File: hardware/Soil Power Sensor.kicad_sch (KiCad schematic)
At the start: 0 parts

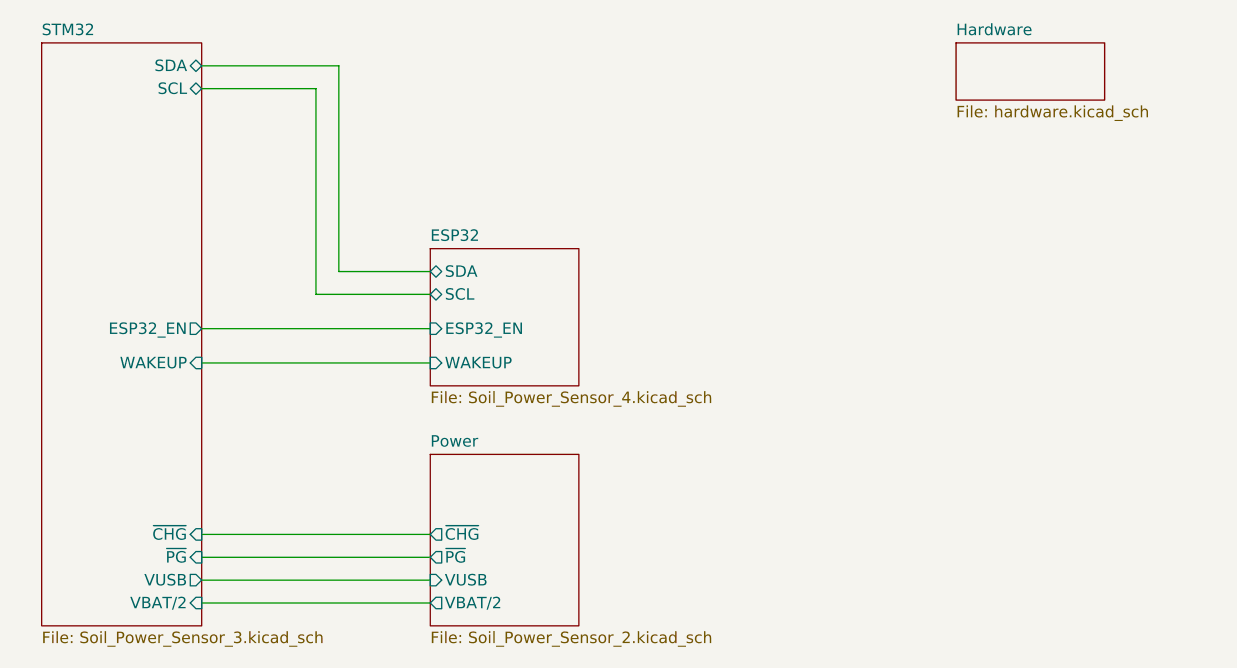
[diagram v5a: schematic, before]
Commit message: lower power buck-boost
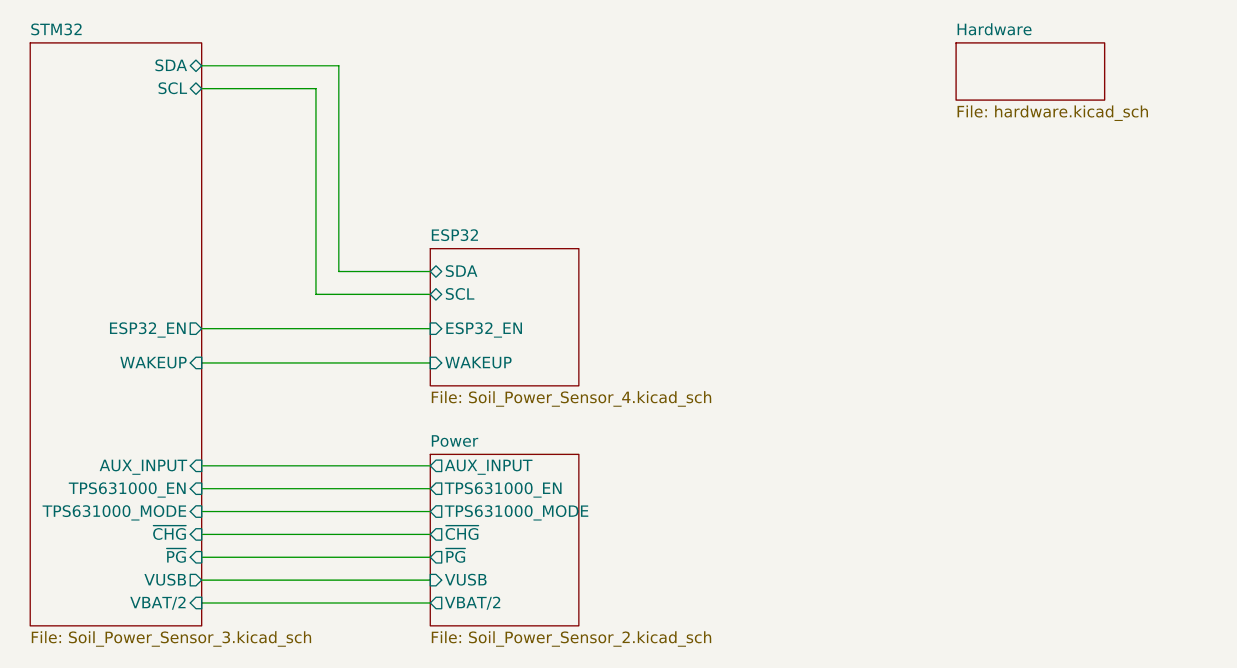
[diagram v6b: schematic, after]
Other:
- sheet Power ports: added AUX_INPUT, TPS631000_EN, TPS631000_MODE; removed none
- sheet STM32 ports: added AUX_INPUT, TPS631000_EN, TPS631000_MODE; removed none
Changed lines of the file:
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@@
+	(wire
+		(pts
+			(xy 137.16 119.38) (xy 162.56 119.38)
+		)
+		(stroke
+			(width 0)
+			(type default)
+		)
+	)
 	(wire
 		(pts
@@
 	(wire
 		(pts
+			(xy 137.16 121.92) (xy 162.56 121.92)
+		)
+		(stroke
+			(width 0)
+			(type default)
+		)
+	)
+	(wire
+		(pts
 			(xy 162.56 100.33) (xy 149.86 100.33)
 		)
@@
 		(pts
 			(xy 137.16 74.93) (xy 152.4 74.93)
+		)
+		(stroke
+			(width 0)
+			(type default)
+		)
+	)
+	(wire
+		(pts
+			(xy 137.16 124.46) (xy 162.56 124.46)
 		)
 		(stroke
@@
 	)
 	(sheet
-		(at 119.38 72.39)
-		(size 17.78 64.77)
+		(at 118.11 72.39)
+		(size 19.05 64.77)
 		(exclude_from_sim no)
 		(in_bom yes)
@@
 		)
 		(property "Sheetname" "STM32"
-			(at 119.38 71.6784 0)
+			(at 118.11 71.6784 0)
 			(effects
 				(font
@@
 		)
 		(property "Sheetfile" "Soil_Power_Sensor_3.kicad_sch"
-			(at 119.38 137.7446 0)
+			(at 118.11 137.7446 0)
 			(effects
 				(font
@@
 		(pin "VBAT{slash}2" input
 			(at 137.16 134.62 0)
+			(effects
+				(font
+					(size 1.27 1.27)
+				)
+				(justify right)
+			)
+		)
+		(pin "TPS631000_EN" input
+			(at 137.16 121.92 0)
+			(effects
+				(font
+					(size 1.27 1.27)
+				)
+				(justify right)
+			)
+		)
+		(pin "TPS631000_MODE" input
+			(at 137.16 124.46 0)
+			(effects
+				(font
+					(size 1.27 1.27)
+				)
+				(justify right)
+			)
+		)
+		(pin "AUX_INPUT" input
+			(at 137.16 119.38 0)
 			(effects
 				(font
@@
 			(effects
 				(font
+					(size 1.27 1.27)
+				)
+				(justify left)
+			)
+		)
+		(pin "TPS631000_EN" output
+			(at 162.56 121.92 180)
+			(effects
+				(font
+					(size 1.27 1.27)
+				)
+				(justify left)
+			)
+		)
+		(pin "TPS631000_MODE" output
+			(at 162.56 124.46 180)
+			(effects
+				(font
+					(size 1.27 1.27)
+				)
+				(justify left)
+			)
+		)
+		(pin "AUX_INPUT" output
+			(at 162.56 119.38 180)
+			(effects
+				(font

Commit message: rough layout spacing
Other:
- sheet Power ports: added SOLAR_DETECT; removed AUX_INPUT
- sheet STM32 ports: added SOLAR_DETECT; removed AUX_INPUT
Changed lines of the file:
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@@
 			)
 		)
-		(pin "WAKEUP" input
+		(pin "WAKEUP" output
 			(at 137.16 107.95 0)
 			(effects
@@
 			)
 		)
-		(pin "AUX_INPUT" input
+		(pin "SOLAR_DETECT" input
 			(at 137.16 119.38 0)
 			(effects
@@
 			)
 		)
-		(pin "AUX_INPUT" output
+		(pin "SOLAR_DETECT" output
 			(at 162.56 119.38 180)
 			(effects

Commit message: finishing touches and fabrication output
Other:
- sheet Power ports: added none; removed TPS631000_EN, TPS631000_MODE
- sheet STM32 ports: added none; removed TPS631000_EN, TPS631000_MODE
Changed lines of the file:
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@@
 	(title_block
 		(title "Soil Power Sensor")
-		(date "2024-12-07")
-		(rev "2.2.3")
+		(date "2026-03-13")
+		(rev "3.0.0")
 		(company "jlab")
 	)
@@
 	(wire
 		(pts
-			(xy 137.16 119.38) (xy 162.56 119.38)
+			(xy 137.16 124.46) (xy 162.56 124.46)
 		)
 		(stroke
@@
 	(wire
 		(pts
-			(xy 137.16 121.92) (xy 162.56 121.92)
-		)
-		(stroke
-			(width 0)
-			(type default)
-		)
-	)
-	(wire
-		(pts
-			(xy 162.56 100.33) (xy 149.86 100.33)
-		)
-		(stroke
-			(width 0)
-			(type default)
-		)
-	)
-	(wire
-		(pts
 			(xy 137.16 134.62) (xy 162.56 134.62)
 		)
@@
 	(wire
 		(pts
-			(xy 137.16 74.93) (xy 152.4 74.93)
-		)
-		(stroke
-			(width 0)
-			(type default)
-		)
-	)
-	(wire
-		(pts
-			(xy 137.16 124.46) (xy 162.56 124.46)
-		)
-		(stroke
-			(width 0)
-			(type default)
-		)
-	)
-	(wire
-		(pts
-			(xy 137.16 77.47) (xy 149.86 77.47)
+			(xy 137.16 97.79) (xy 162.56 97.79)
+		)
+		(stroke
+			(width 0)
+			(type default)
+		)
+	)
+	(wire
+		(pts
+			(xy 137.16 100.33) (xy 162.56 100.33)
 		)
 		(stroke
@@
 		(pts
 			(xy 137.16 132.08) (xy 162.56 132.08)
-		)
-		(stroke
-			(width 0)
-			(type default)
-		)
-	)
-	(wire
-		(pts
-			(xy 149.86 77.47) (xy 149.86 100.33)
-		)
-		(stroke
-			(width 0)
-			(type default)
-		)
-	)
-	(wire
-		(pts
-			(xy 162.56 97.79) (xy 152.4 97.79)
-		)
-		(stroke
-			(width 0)
-			(type default)
-		)
-	)
-	(wire
-		(pts
-			(xy 152.4 74.93) (xy 152.4 97.79)
 		)
 		(stroke
@@
 	)
 	(sheet
-		(at 118.11 72.39)
-		(size 19.05 64.77)
+		(at 118.11 95.25)
+		(size 19.05 41.91)
 		(exclude_from_sim no)
 		(in_bom yes)
@@
 		)
 		(property "Sheetname" "STM32"
-			(at 118.11 71.6784 0)
+			(at 118.11 94.5384 0)
 			(effects
 				(font
@@
 		)
 		(pin "SDA" bidirectional
-			(at 137.16 74.93 0)
+			(at 137.16 97.79 0)
 			(effects
 				(font
@@
 		)
 		(pin "SCL" bidirectional
-			(at 137.16 77.47 0)
+			(at 137.16 100.33 0)
 			(effects
 				(font
@@
 			)
 		)
-		(pin "TPS631000_EN" input
-			(at 137.16 121.92 0)
-			(effects
-				(font
-					(size 1.27 1.27)
-				)
-				(justify right)
-			)
-		)
-		(pin "TPS631000_MODE" input
+		(pin "SOLAR_DETECT" input
 			(at 137.16 124.46 0)
-			(effects
-				(font
-					(size 1.27 1.27)
-				)
-				(justify right)
-			)
-		)
-		(pin "SOLAR_DETECT" input
-			(at 137.16 119.38 0)
 			(effects
 				(font
@@
 	)
 	(sheet
-		(at 162.56 118.11)
-		(size 16.51 19.05)
+		(at 162.56 121.92)
+		(size 16.51 15.24)
 		(exclude_from_sim no)
 		(in_bom yes)
@@
 		)
 		(property "Sheetname" "Power"
-			(at 162.56 117.3984 0)
+			(at 162.56 121.2084 0)
 			(effects
 				(font
@@
 			)
 		)
-		(pin "TPS631000_EN" output
-			(at 162.56 121.92 180)
-			(effects
-				(font
-					(size 1.27 1.27)
-				)
-				(justify left)
-			)
-		)
-		(pin "TPS631000_MODE" output
+		(pin "SOLAR_DETECT" output
 			(at 162.56 124.46 180)
-			(effects
-				(font
-					(size 1.27 1.27)
-				)
-				(justify left)
-			)
-		)
-		(pin "SOLAR_DETECT" output
-			(at 162.56 119.38 180)
 			(effects
 				(font
@@
 	)
 	(sheet
-		(at 220.98 72.39)
+		(at 204.47 95.25)
 		(size 16.51 6.35)
 		(exclude_from_sim no)
@@
 		)
 		(property "Sheetname" "Hardware"
-			(at 220.98 71.6784 0)
+			(at 204.47 94.5384 0)
 			(effects
 				(font
@@
 		)
 		(property "Sheetfile" "hardware.kicad_sch"
-			(at 220.98 79.3246 0)
-			(effects
-				(font
+			(at 204.47 102.1846 0)
+			(effects
+				(font
